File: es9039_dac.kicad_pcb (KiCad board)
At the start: 4 copper layers, 82.2 x 55.9 mm, 103 parts, among them J1 Conn_02x07_Odd_Even, J2 RCA_L, J3 XLR_R, J4 RCA_R, J5 XLR_L, J6 BAL_OUT, J7 UNBAL_OUT, U1 ES9039Q2M, U2 TPS7A2033DBV, U3 LP5912-3.3DRV, U4 LP5912-3.3DRV, U5 TPS7A2033DBV, U6 OPA1612AxD, U7 OPA1612AxD, U8 OPA1612AxD, U9 OPA1612AxD

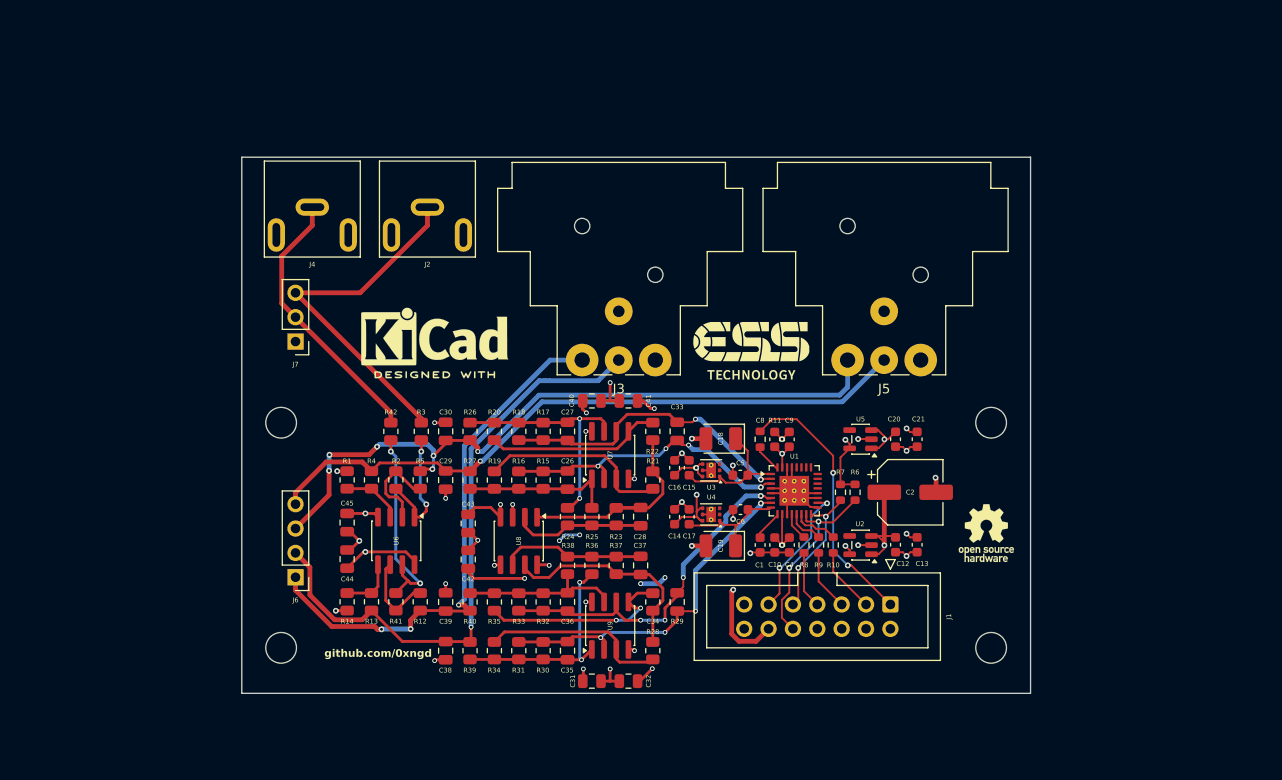
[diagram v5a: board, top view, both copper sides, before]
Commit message: add oscillator
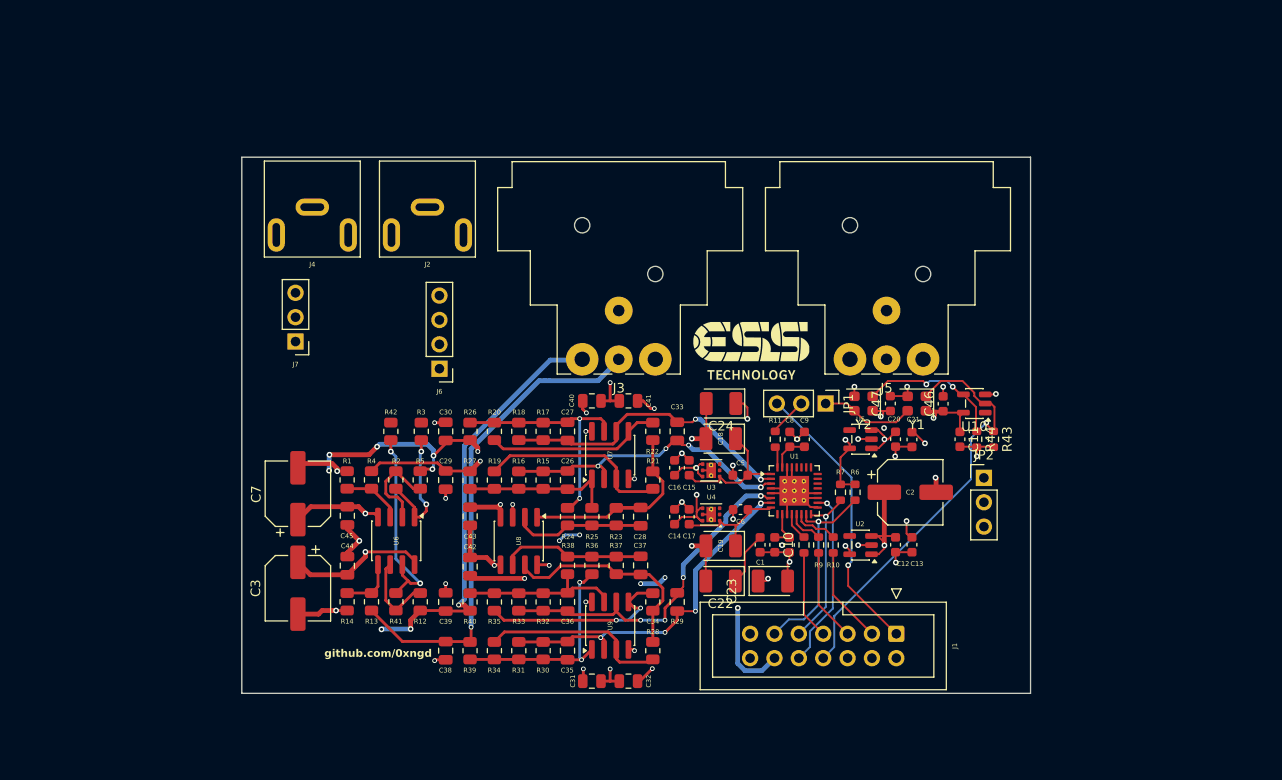
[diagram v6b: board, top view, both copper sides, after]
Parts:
- removed REF**: KiCad-Logo2_6mm_SilkScreen, Symbol:KiCad-Logo2_6mm_SilkScreen
- removed REF** (x4): MountingHole_3.2mm_M3, MountingHole:MountingHole_3.2mm_M3
- removed REF**: OSHW-Logo_5.7x6mm_SilkScreen, Symbol:OSHW-Logo_5.7x6mm_SilkScreen
- added C11: 100n, Capacitor_SMD:C_0603_1608Metric, F.Cu at (237.8, 89.7)
- added C22: 47u, Capacitor_Tantalum_SMD:CP_EIA-3528-12_Kemet-T, F.Cu at (212.8, 104.5)
- added C23: 47u, Capacitor_Tantalum_SMD:CP_EIA-3528-12_Kemet-T, F.Cu at (218.2, 104.5)
- added C24: 47u, Capacitor_Tantalum_SMD:CP_EIA-3528-12_Kemet-T, F.Cu at (212.8, 86.0)
- added C3: 100u, Capacitor_SMD:CP_Elec_6.3x5.8, F.Cu at (168.8, 105.2)
- added C46: 100n, Capacitor_SMD:C_0603_1608Metric, F.Cu at (236.0, 86.0)
- added C47: 100n, Capacitor_SMD:C_0603_1608Metric, F.Cu at (230.5, 86.0)
- added C7: 100u, Capacitor_SMD:CP_Elec_6.3x5.8, F.Cu at (168.8, 95.4)
- added JP1: MCLK_JUMPER, Connector_PinHeader_2.54mm:PinHeader_1x03_P2.54mm_Vertical, F.Cu at (223.8, 86.0)
- added JP2: MCLK_JUMPER_PWR, Connector_PinHeader_2.54mm:PinHeader_1x03_P2.54mm_Vertical, F.Cu at (240.2, 93.8)
- added R43: 10K, Resistor_SMD:R_0603_1608Metric, F.Cu at (241.2, 89.7)
- added R44: 10K, Resistor_SMD:R_0603_1608Metric, F.Cu at (239.5, 89.7)
- added U10: SN74LVC1G14DBV, Package_TO_SOT_SMD:SOT-23-5, F.Cu at (239.2, 86.0)
- added Y1: 45.1584MHz, Oscillator:Oscillator_SMD_SiT_PQFN-4Pin_2.5x2.0mm, F.Cu at (233.2, 86.0)
- added Y2: 45.1584MHz, Oscillator:Oscillator_SMD_SiT_PQFN-4Pin_2.5x2.0mm, F.Cu at (227.7, 86.0)
- moved J6 26.4 mm to (183.5, 82.4)
- moved J1 3.12 mm to (231.1, 110.0)
- moved C8 1.57 mm to (220.0, 89.7)
- moved C9 1.57 mm to (221.5, 89.7)
- moved R11 1.57 mm to (218.5, 89.7)
- moved C42 0.78 mm to (186.7, 103.0)
- moved C43 0.78 mm to (186.7, 97.8)
- moved C45 0.71 mm to (173.9, 97.7)
- moved C44 0.68 mm to (173.9, 102.9)
- moved C21 0.54 mm to (232.8, 89.8)
- moved C13 0.54 mm to (232.8, 100.7)
- moved J5 0.26 mm to (233.9, 81.4)
- moved J3 0.08 mm to (206.0, 81.4)
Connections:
- J1 pad 1: /I2S_MCLK -> /AMANERO_MCLK
- J1 pad 10: /I2C_SCL -> /DAC_STBY
- J1 pad 11: /DAC_STBY -> /I2C_SCL
- J1 pad 8: GNDA -> /FREQ_SEL
- R11 pad 1: /I2S_MCLK -> /DAC_MCLK
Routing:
- net OUT_L: track 69.8 -> 12.5 mm
- net OUT_Lb: track 74.4 -> 22.8 mm
- net /FREQ_SEL: track 0.00 -> 44.5 mm, vias 0 -> 1
- net UNBAL_OUT_L: track 37.5 -> 0.00 mm
- net GNDA: track 72.9 -> 105.1 mm, vias 25 -> 29
- net /AMANERO_MCLK: track 0.00 -> 29.5 mm, vias 0 -> 1
- net UNBAL_OUT_R: track 28.5 -> 0.00 mm
- net /I2S_MCLK: track 27.9 -> 0.00 mm, vias 2 -> 0
- net +3.3VCLK: track 0.00 -> 25.3 mm, vias 0 -> 2
- net +3.3V: track 25.9 -> 45.6 mm, vias 3 -> 4
- net Net-(Y2-OE): track 0.00 -> 15.4 mm, vias 0 -> 2
- net OUT_R: track 63.9 -> 51.0 mm
- net OUT_Rb: track 57.4 -> 45.4 mm
- net /CRYSTAL_MCLK: track 0.00 -> 9.86 mm
- net +12V: track 95.1 -> 102.7 mm
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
